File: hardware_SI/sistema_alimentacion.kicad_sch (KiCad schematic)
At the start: 30 parts, among them J1 Barrel_Jack_Switch, Q1 SI2323DS-T1, Q2 SI2323DS-T1, SW1 SW_SPDT, U2 LTC4085EDEPBF, U3 TPS61200DRC, U4 LD1117S33TR_SOT223

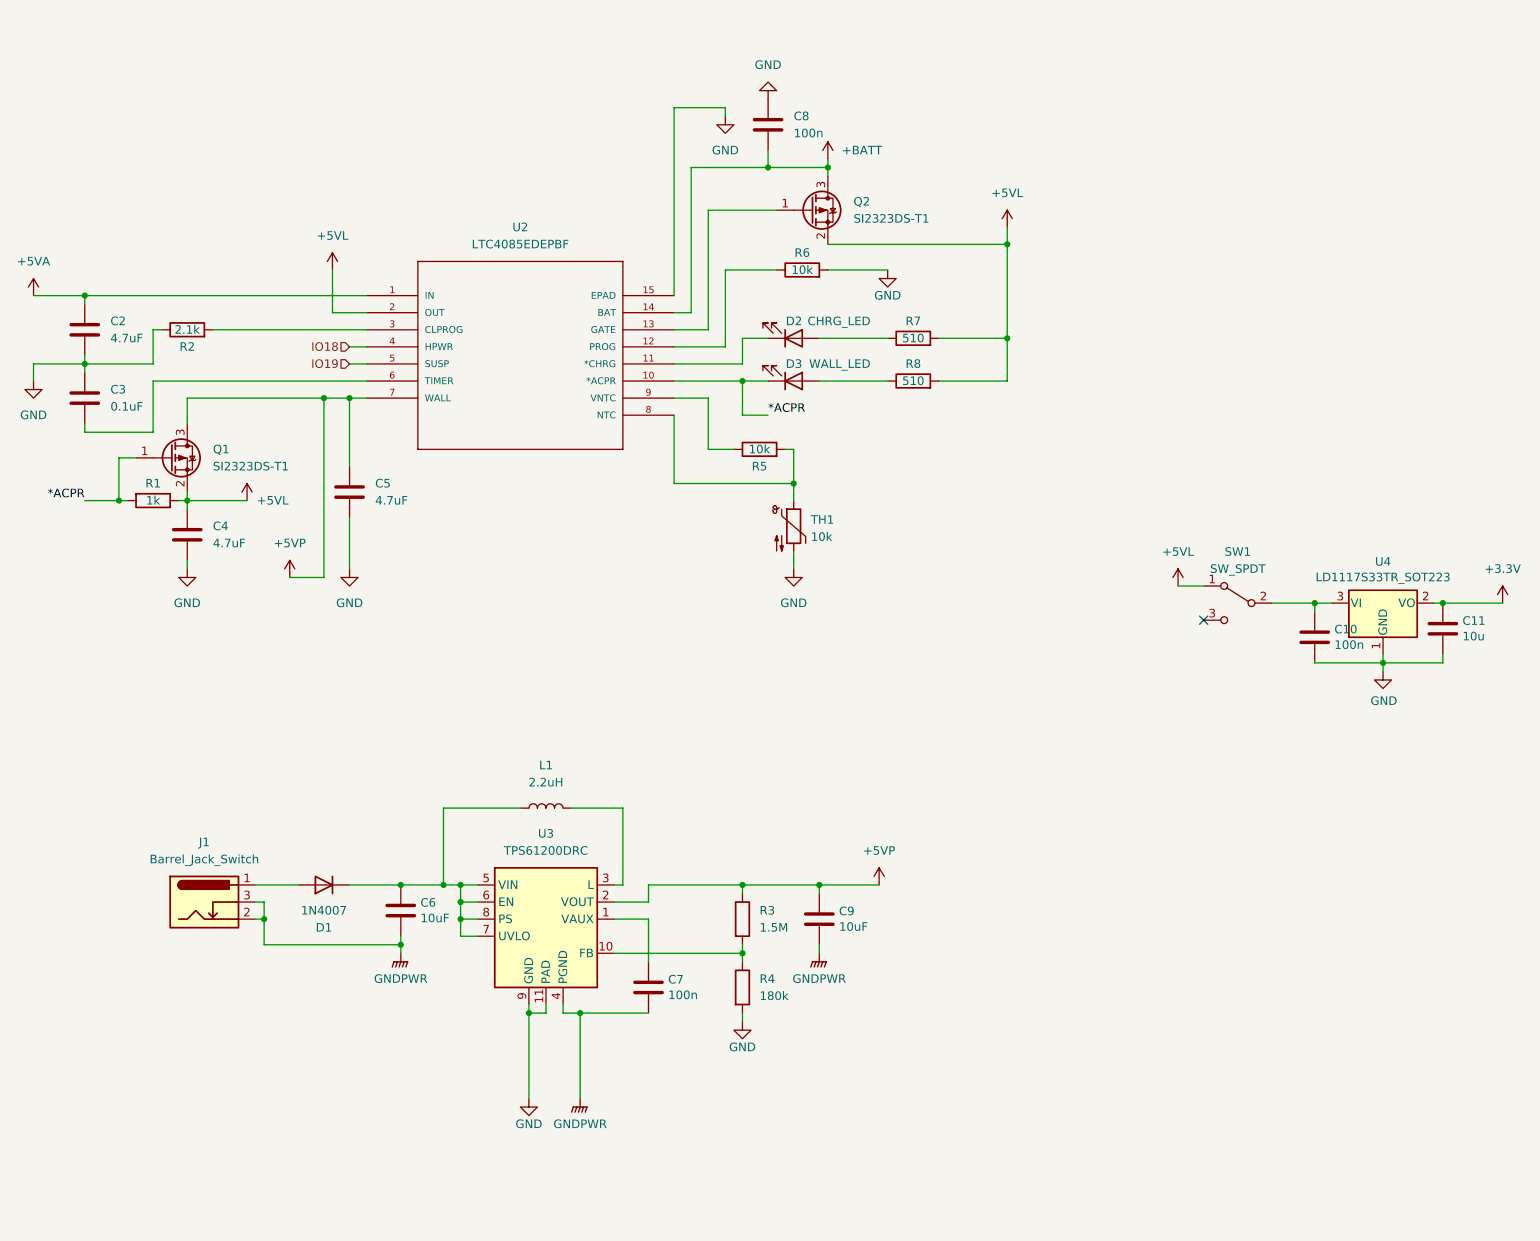
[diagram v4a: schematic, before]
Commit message: Cambio en alimentación y zona GNDPWR
- Debido a los tiempos de entrega del LTC4085, se cambia el sistema de alimentación, agregando un selector automático de fuente y un integrado de manejo de batería.
- En consecuencia de lo anterior, se usa un LDO con menor voltaje de dropout.
- Se cambia el convertidor DC-DC debido a su alto precio.
- En cuanto a PCB, se completa el circuito del convertidor DC-DC y la zona de GNPWR.
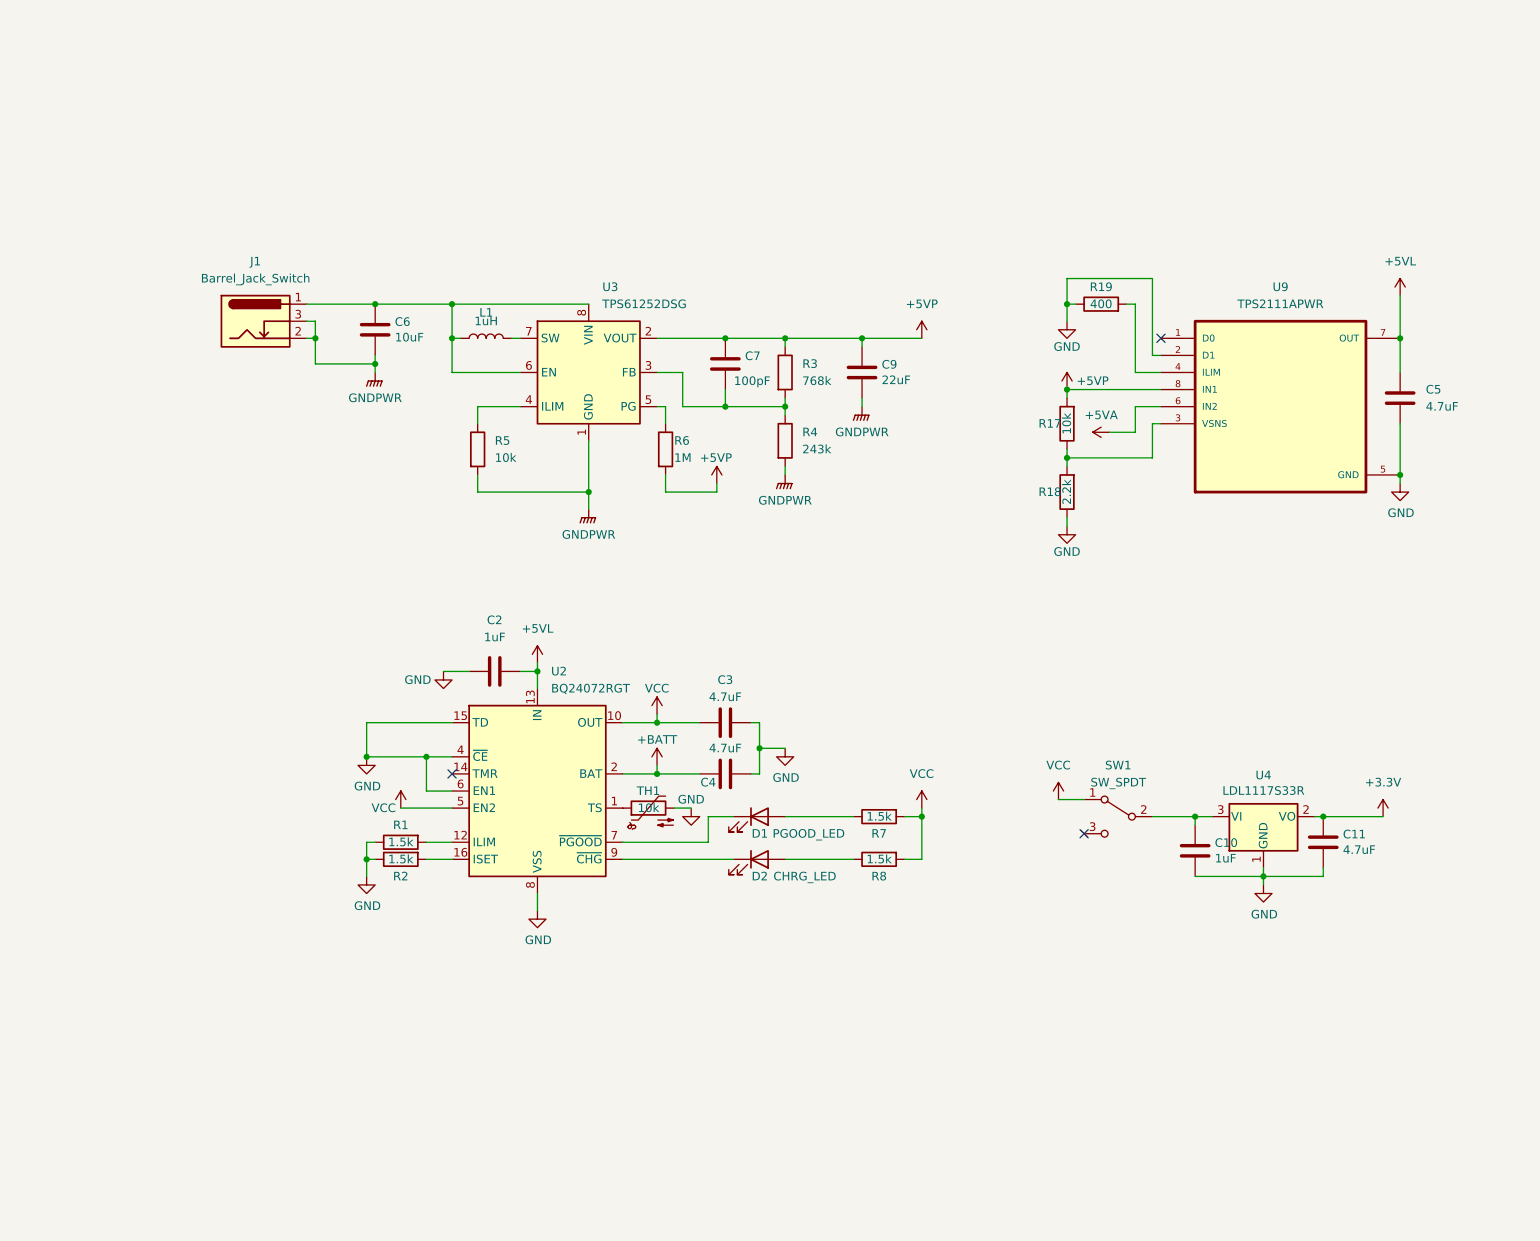
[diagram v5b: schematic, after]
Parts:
- removed C8: 100n, Capacitor_SMD:C_0805_2012Metric_Pad1.18x1.45mm_HandSolder, symbol Device:C
- removed D1: 1N4007, Diode_SMD:D_SMA_Handsoldering, symbol Diode:1N4007
- removed D3: WALL_LED, LED_SMD:LED_0805_2012Metric_Pad1.15x1.40mm_HandSolder, symbol Device:LED
- removed Q1, Q2: SI2323DS-T1, Package_TO_SOT_SMD:SOT-23_Handsoldering, symbol Device:Q_PMOS_GSD
- removed U2: LTC4085EDEPBF, LTC4085EDEPBF:DFN-14_DE, symbol LTC4085EDEPBF:LTC4085EDEPBF
- removed U3: TPS61200DRC, Package_SON:Texas_S-PVSON-N10_ThermalVias, symbol Regulator_Switching:TPS61200DRC
- added D1: PGOOD_LED, LED_SMD:LED_0805_2012Metric_Pad1.15x1.40mm_HandSolder, symbol Device:LED
- added R17: 10k, Resistor_SMD:R_0805_2012Metric_Pad1.20x1.40mm_HandSolder, symbol Device:R
- added R18: 2.2k, Resistor_SMD:R_0805_2012Metric_Pad1.20x1.40mm_HandSolder, symbol Device:R
- added R19: 400, Resistor_SMD:R_0805_2012Metric_Pad1.20x1.40mm_HandSolder, symbol Device:R
- added U2: BQ24072RGT, Package_DFN_QFN:VQFN-16-1EP_3x3mm_P0.5mm_EP1.6x1.6mm, symbol Battery_Management:BQ24072RGT
- added U3: TPS61252DSG, Package_SON:WSON-8-1EP_2x2mm_P0.5mm_EP0.9x1.6mm, symbol Regulator_Switching:TPS61252DSG
- added U9: TPS2111APWR, SOP65P640X120-8N, symbol TPS2111APWR:TPS2111APWR
- C10: value 100n -> 1uF
- C11: value 10u -> 4.7uF
- C2: value 4.7uF -> 1uF
- C3: value 0.1uF -> 4.7uF
- C7: value 100n -> 100pF
- C9: value 10uF -> 22uF
- L1: value 2.2uH -> 1uH; footprint Inductor_SMD:L_Coilcraft_LPS4018 -> Inductor_SMD:L_Bourns-SRN4018
- R1: value 1k -> 1.5k
- R2: value 2.1k -> 1.5k
- R3: value 1.5M -> 768k
- R4: value 180k -> 243k
- R6: value 10k -> 1M
- R7, R8: value 510 -> 1.5k
- U4: value LD1117S33TR_SOT223 -> LDL1117S33R
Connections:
- net +5VA: now also U9.6 (IN2); no longer C2.1
- net +5VL: now also C2.2, C5.1, U2.13 (IN), U9.7 (OUT); no longer C4.1, R1.1, R7.2, R8.2, SW1.1 (A)
- net +5VP: now also C7.1, R6.2, R17.2, U3.2 (VOUT), U9.8 (IN1); no longer C5.1
- net +BATT: now also C4.1, U2.2 (BAT), U2.3 (BAT)
- net GND: now also C2.1, R1.1, R18.1, R19.1, U2.15 (TD), U2.17 (VSS), U2.4 (~{CE}), U2.6 (EN1), U2.8 (VSS), U9.2 (D1), U9.5 (GND); no longer C2.2, R4.2, R6.2
- net GNDPWR: now also R4.2, R5.2, U3.1 (GND), U3.9 (GND); no longer C7.2
- net at TH1.1: now also U2.1 (TS); no longer R5.2
- net at D2.1 (K): now also U2.9 (~{CHG})
- net at R6.1: now also U3.5 (PG)
- net at R2.2: now also U2.16 (ISET)
- net VCC: now reaches C3.1
- net VCC: now also R7.2, R8.2, SW1.1 (A), U2.10 (OUT), U2.11 (OUT), U2.5 (EN2)
- net at R5.1: now also U3.4 (ILIM)
- net at R3.2, R4.1: now also C7.2, U3.3 (FB)
- net at L1.2: now also U3.7 (SW)
- net at C6.1, L1.1: now also J1.1, U3.6 (EN), U3.8 (VIN)
- net at R8.1: now also D2.2 (A)
- net at R7.1: now also D1.2 (A); no longer D2.2 (A)
- net *ACPR: no longer names the net of R1.2
- net *ACPR: now also U2.12 (ILIM)
- new net: D1.1 (K), U2.7 (~{PGOOD})
- new net: R17.1, R18.2, U9.3 (VSNS)
- new net: R19.2, U9.4 (ILIM)
- no-connect marks 1 -> 3
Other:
- moved on the sheet: C10, C11, C6, C7, C9, J1, L1, R3, R4, SW1, U4

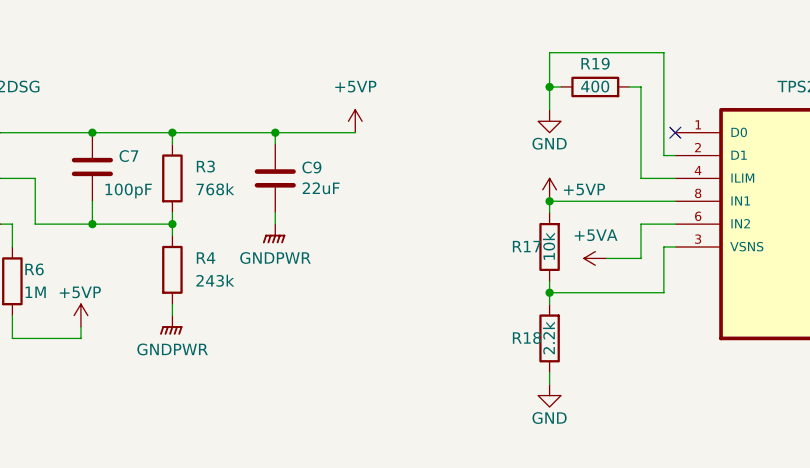
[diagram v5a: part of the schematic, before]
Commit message: Archivos de fabricación y cambios menores
- Se generan los archivos de fabricación.
- Se cambian algunas resistencias por valores más comerciales.
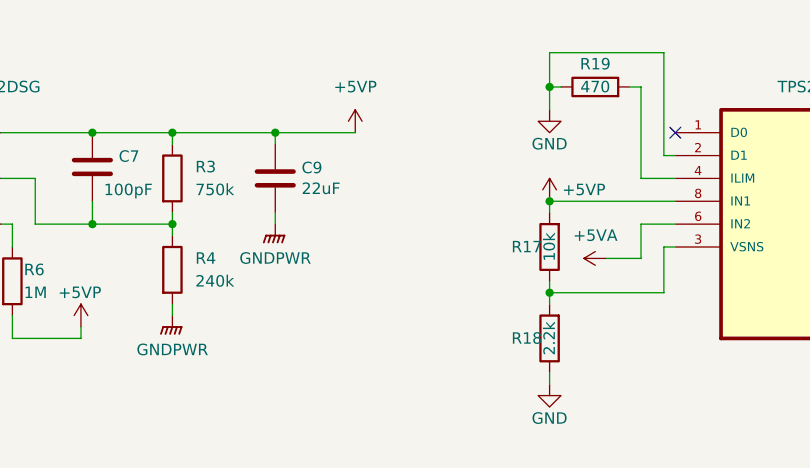
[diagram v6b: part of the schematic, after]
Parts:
- R19: value 400 -> 470
- R3: value 768k -> 750k; footprint Resistor_SMD:R_0805_2012Metric_Pad1.20x1.40mm_HandSolder -> Resistor_SMD:R_0603_1608Metric_Pad0.98x0.95mm_HandSolder
- R4: value 243k -> 240k; footprint Resistor_SMD:R_0805_2012Metric_Pad1.20x1.40mm_HandSolder -> Resistor_SMD:R_0603_1608Metric_Pad0.98x0.95mm_HandSolder
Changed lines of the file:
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@@
       (effects (font (size 1.27 1.27)) (justify left))
     )
-    (property "Value" "768k" (id 1) (at 144.78 68.5799 0)
+    (property "Value" "750k" (id 1) (at 144.78 68.5799 0)
       (effects (font (size 1.27 1.27)) (justify left))
     )
-    (property "Footprint" "Resistor_SMD:R_0805_2012Metric_Pad1.20x1.40mm_HandSolder" (id 2) (at 140.462 67.31 90)
+    (property "Footprint" "Resistor_SMD:R_0603_1608Metric_Pad0.98x0.95mm_HandSolder" (id 2) (at 140.462 67.31 90)
       (effects (font (size 1.27 1.27)) hide)
     )
@@
     (in_bom yes) (on_board yes)
     (property "Reference" "R19" (id 0) (at 189.23 54.61 90))
-    (property "Value" "400" (id 1) (at 189.23 57.15 90))
+    (property "Value" "470" (id 1) (at 189.23 57.15 90))
     (property "Footprint" "Resistor_SMD:R_0805_2012Metric_Pad1.20x1.40mm_HandSolder" (id 2) (at 189.23 58.928 90)
       (effects (font (size 1.27 1.27)) hide)
@@
       (effects (font (size 1.27 1.27)) (justify left))
     )
-    (property "Value" "243k" (id 1) (at 144.78 78.7399 0)
+    (property "Value" "240k" (id 1) (at 144.78 78.7399 0)
       (effects (font (size 1.27 1.27)) (justify left))
     )
-    (property "Footprint" "Resistor_SMD:R_0805_2012Metric_Pad1.20x1.40mm_HandSolder" (id 2) (at 140.462 77.47 90)
+    (property "Footprint" "Resistor_SMD:R_0603_1608Metric_Pad0.98x0.95mm_HandSolder" (id 2) (at 140.462 77.47 90)
       (effects (font (size 1.27 1.27)) hide)
     )
